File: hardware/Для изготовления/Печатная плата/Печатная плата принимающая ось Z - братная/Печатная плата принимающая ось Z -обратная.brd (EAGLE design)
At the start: 32.4 x 38.1 mm, 10 parts, among them J1 22-03-5035

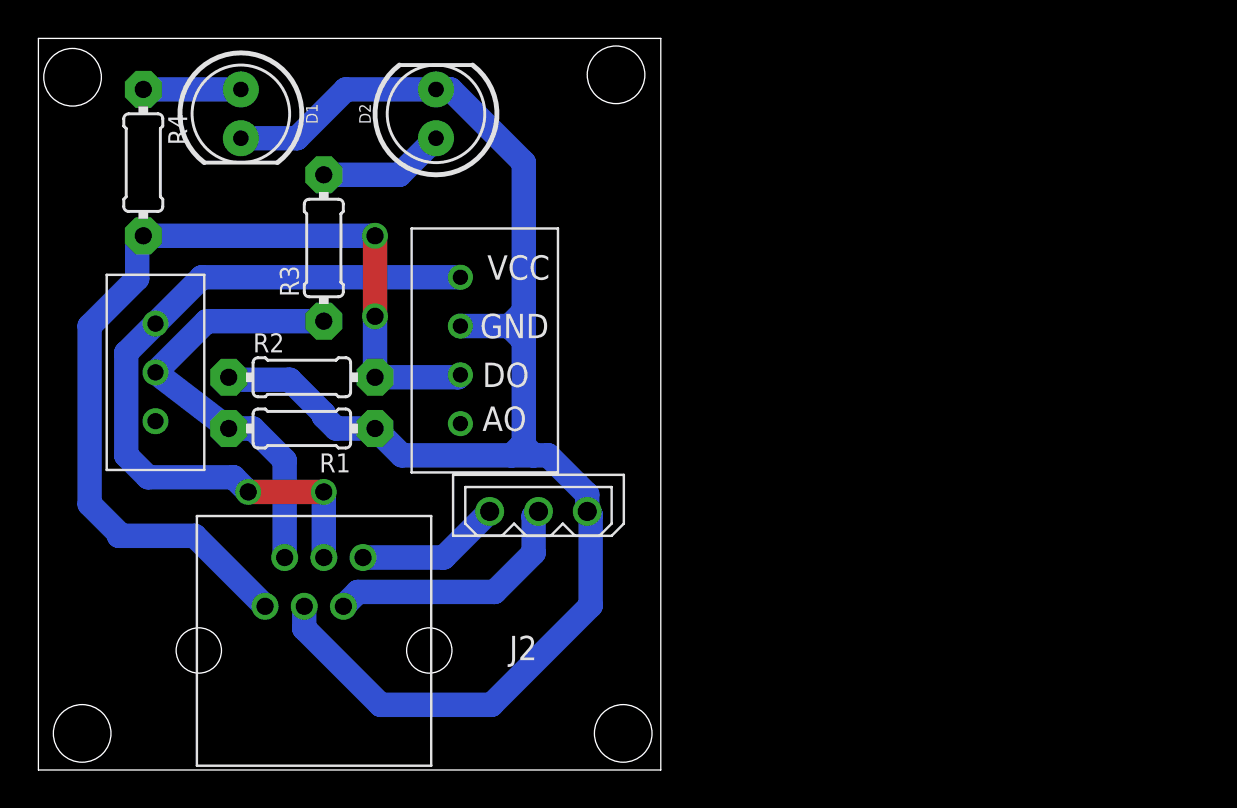
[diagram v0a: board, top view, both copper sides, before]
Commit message: Добавлена отзеркаленная принимающая плата оси Z
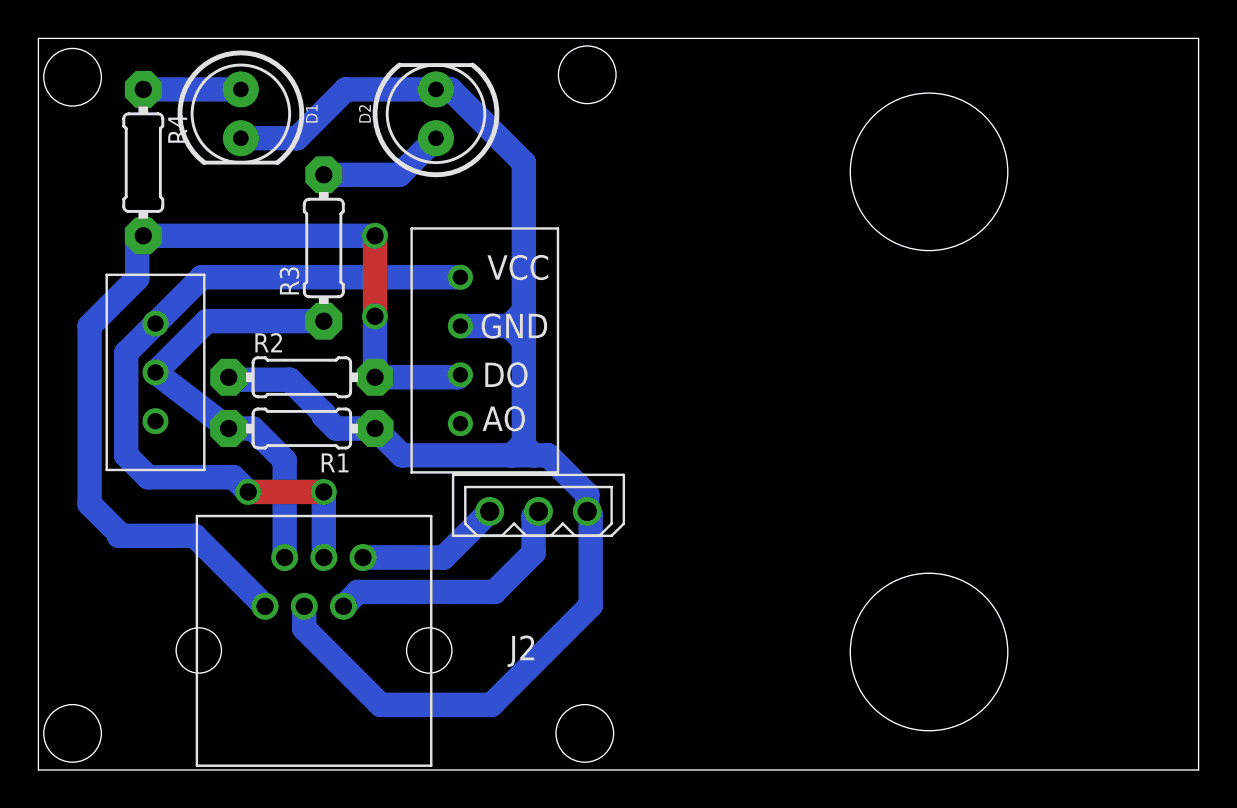
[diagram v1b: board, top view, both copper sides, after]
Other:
- board size 32.4 x 38.1 mm -> 60.4 x 38.1 mm
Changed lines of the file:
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@@
 <drawing>
 <settings>
-<setting alwaysvectorfont="no"/>
+<setting alwaysvectorfont="yes"/>
 <setting verticaltext="up"/>
 </settings>
-<grid distance="1" unitdist="mm" unit="mm" style="lines" multiple="1" display="no" altdistance="0.5" altunitdist="mm" altunit="mm"/>
+<grid distance="10" unitdist="mm" unit="mm" style="lines" multiple="1" display="no" altdistance="2.5" altunitdist="mm" altunit="mm"/>
 <layers>
 <layer number="1" name="Top" color="4" fill="1" visible="yes" active="yes"/>
@@
 <board>
 <plain>
-<wire x1="16.129" y1="-1.143" x2="48.533" y2="-1.143" width="0" layer="20"/>
-<wire x1="48.533" y1="-1.143" x2="48.533" y2="36.947" width="0" layer="20"/>
-<wire x1="48.533" y1="36.947" x2="16.129" y2="36.947" width="0" layer="20"/>
+<wire x1="16.129" y1="-1.143" x2="76.533" y2="-1.143" width="0" layer="20"/>
+<wire x1="76.533" y1="-1.143" x2="76.533" y2="36.947" width="0" layer="20"/>
+<wire x1="76.533" y1="36.947" x2="16.129" y2="36.947" width="0" layer="20"/>
 <wire x1="16.129" y1="36.947" x2="16.129" y2="-1.143" width="0" layer="20"/>
 <hole x="17.907" y="34.925" drill="3"/>
-<hole x="18.407" y="0.762" drill="3"/>
-<hole x="46.577" y="0.762" drill="3"/>
-<hole x="46.204" y="35.052" drill="3"/>
+<hole x="17.907" y="0.762" drill="3"/>
+<hole x="44.577" y="0.762" drill="3"/>
+<hole x="44.704" y="35.052" drill="3"/>
+<hole x="62.5" y="30" drill="8.2"/>
+<hole x="62.5" y="5" drill="8.2"/>
 </plain>
 <attributes>
